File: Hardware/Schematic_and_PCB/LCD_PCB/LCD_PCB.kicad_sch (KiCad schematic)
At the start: 9 parts, among them J1 LCD_display, J2 Conn_01x03, J4 Conn_01x09, SW1 Button_down, SW2 Button_up, SW3 Button_ok, SW4 Button_back

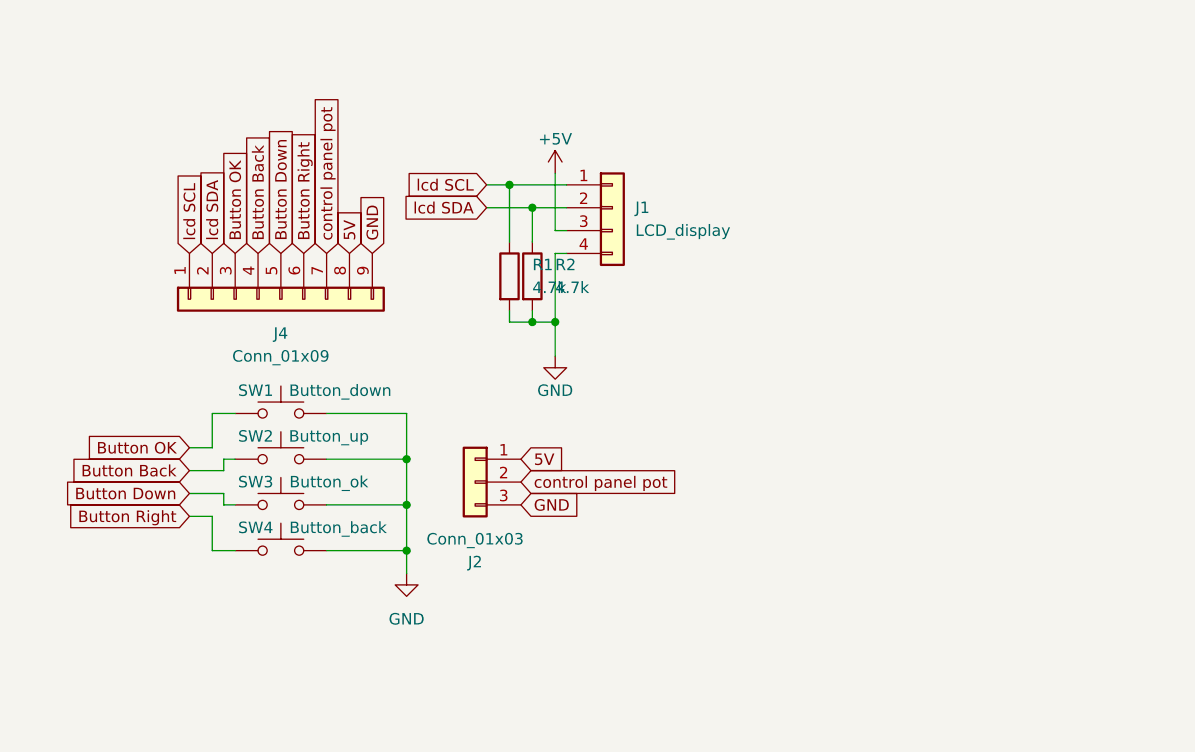
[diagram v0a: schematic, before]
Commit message: Update PCB LCD
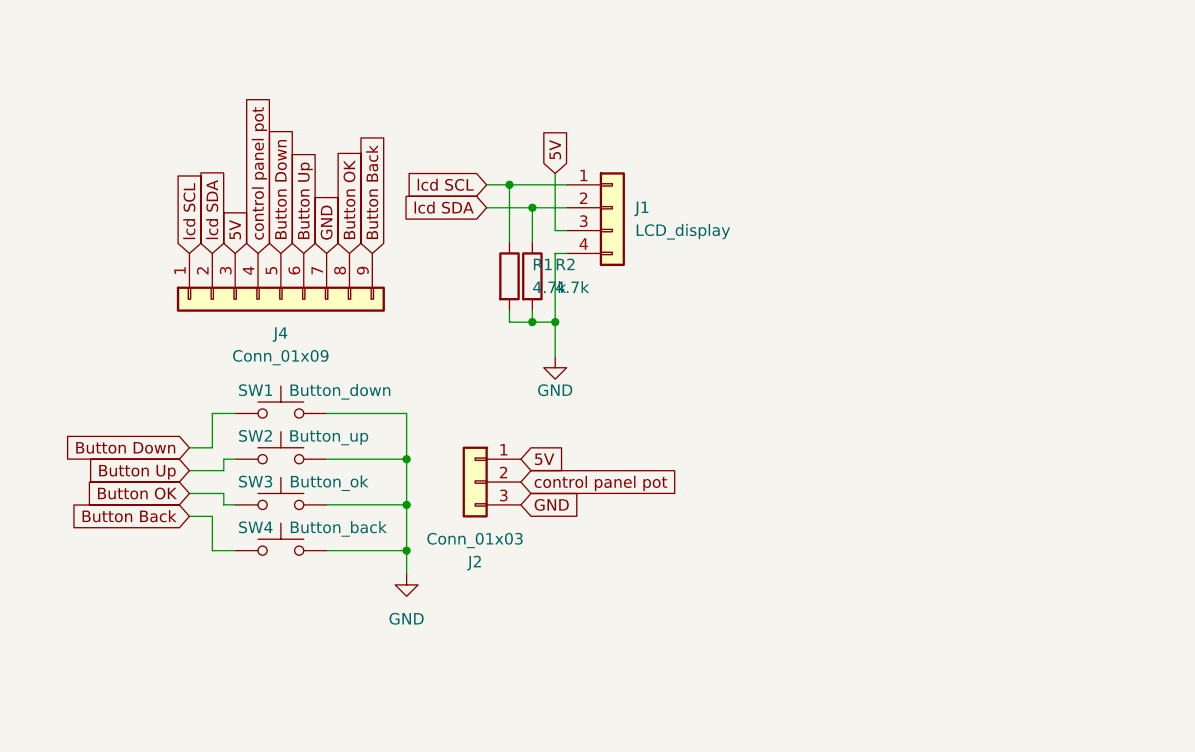
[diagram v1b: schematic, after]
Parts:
- R1, R2: footprint (none) -> Resistor_THT:R_Axial_DIN0207_L6.3mm_D2.5mm_P7.62mm_Horizontal
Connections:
- net +5V is gone; now on net 5V: J1.3 (Pin_3)
- net 5V: now also J4.3 (Pin_3); no longer J4.8 (Pin_8)
- net Button Back: now also J4.9 (Pin_9), SW4.1; no longer J4.4 (Pin_4), SW2.1
- net Button Down: now also SW1.1; no longer SW3.1
- net Button OK: now also J4.8 (Pin_8), SW3.1; no longer J4.3 (Pin_3), SW1.1
- net GND: now also J4.7 (Pin_7); no longer J4.9 (Pin_9)
- net control panel pot: now also J4.4 (Pin_4); no longer J4.7 (Pin_7)
- net Button Right renamed Button Up
- net Button Up: now also SW2.1; no longer SW4.1

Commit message: Finish LCD PCB
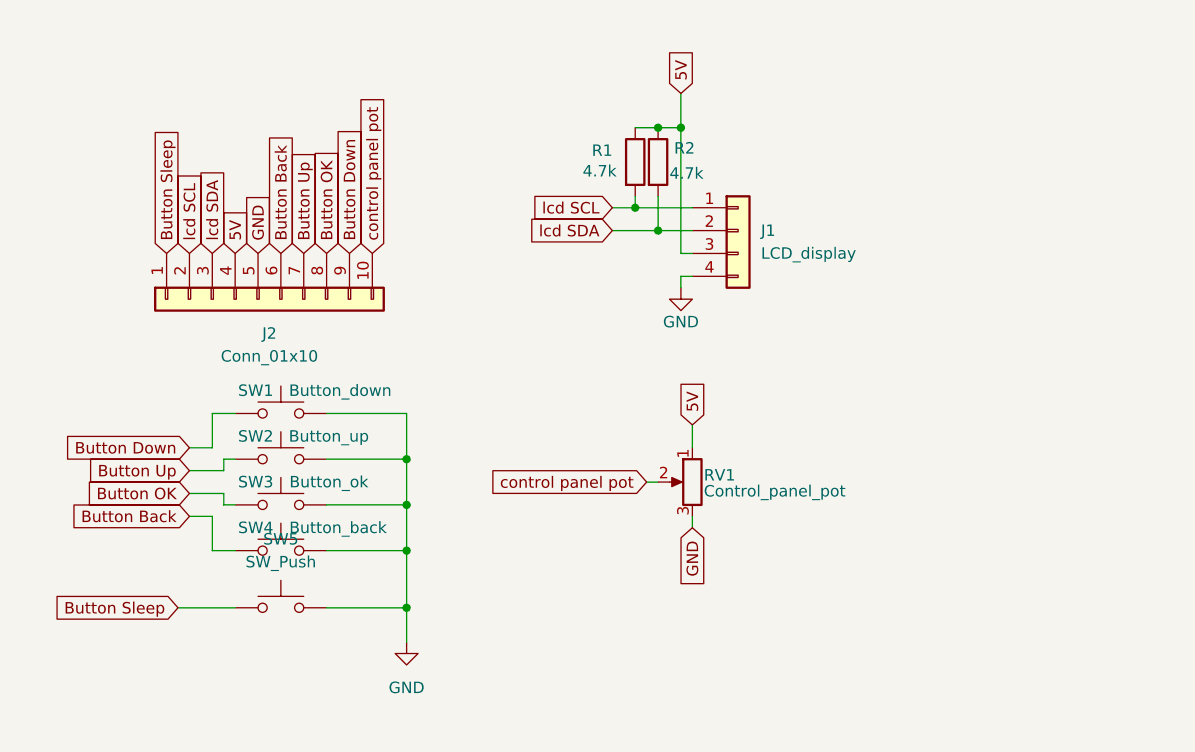
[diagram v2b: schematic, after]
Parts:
- removed J2: Conn_01x03, Connector_PinHeader_2.54mm:PinHeader_1x03_P2.54mm_Vertical, symbol Connector_Generic:Conn_01x03
- removed J4: Conn_01x09, Connector_PinHeader_2.54mm:PinHeader_1x09_P2.54mm_Vertical, symbol Connector_Generic:Conn_01x09
- added J2: Conn_01x10, Connector_PinHeader_2.54mm:PinHeader_1x10_P2.54mm_Vertical, symbol Connector_Generic:Conn_01x10
- added RV1: Control_panel_pot, Potentiometer:PDB182-K-Potentiometer, symbol Device:R_Potentiometer
- added SW5: SW_Push, Button_Switch_THT:SW_PUSH_6mm_H5mm, symbol Switch:SW_Push
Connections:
- net 5V: now also R1.1, R2.1, J2.4 (Pin_4), RV1.1
- net Button Back: now also J2.6 (Pin_6)
- net Button Down: now also J2.9 (Pin_9)
- net Button OK: now also J2.8 (Pin_8)
- net Button Up: now also J2.7 (Pin_7)
- net GND: now also J2.5 (Pin_5), RV1.3, SW5.2; no longer R1.2, R2.2
- net control panel pot: now also J2.10 (Pin_10), RV1.2
- net lcd SCL: now also R1.2, J2.2 (Pin_2); no longer R1.1
- net lcd SDA: now also R2.2, J2.3 (Pin_3); no longer R2.1
- new net Button Sleep: J2.1 (Pin_1), SW5.1
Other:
- moved on the sheet: J1, R1, R2

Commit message: Update bunch of stuff
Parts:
- RV1: footprint Potentiometer:PDB182-K-Potentiometer -> Potentiometer:PDB182-K-Potentiometer-Horizontal
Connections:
- net 5V: now also J2.2 (Pin_2), RV1.3; no longer J2.4 (Pin_4), RV1.1
- net Button Back: now also J2.4 (Pin_4); no longer J2.6 (Pin_6)
- net Button Down: now also J2.5 (Pin_5); no longer J2.9 (Pin_9)
- net Button OK: now also J2.6 (Pin_6); no longer J2.8 (Pin_8)
- net Button Sleep: now also J2.3 (Pin_3); no longer J2.1 (Pin_1)
- net GND: now also J2.8 (Pin_8), RV1.1; no longer J2.5 (Pin_5), RV1.3
- net control panel pot: now also J2.1 (Pin_1); no longer J2.10 (Pin_10)
- net lcd SCL: now also J2.9 (Pin_9); no longer J2.2 (Pin_2)
- net lcd SDA: now also J2.10 (Pin_10); no longer J2.3 (Pin_3)
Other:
- moved on the sheet: RV1

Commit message: Finalize LCD PCB
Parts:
- added H1, H2, H3, H4: MountingHole, MountingHole:MountingHole_3.2mm_M3, symbol Mechanical:MountingHole

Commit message: Code update for room 3
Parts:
- added TP1, TP2, TP3, TP4, TP5, TP6: TestPoint, TestPoint:TestPoint_Pad_1.5x1.5mm, symbol Connector:TestPoint
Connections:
- net 5V: now also TP6.1
- net Button Sleep: now also TP1.1
- net GND: now also TP5.1
- net control panel pot: now also TP2.1
- net lcd SCL: now also TP3.1
- net lcd SDA: now also TP4.1

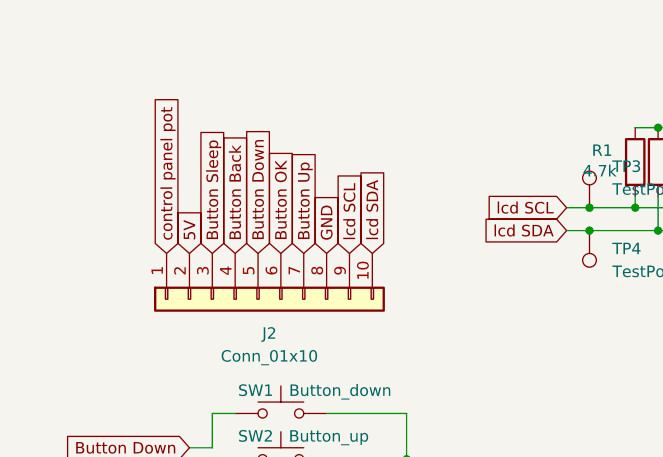
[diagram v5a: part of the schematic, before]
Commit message: Update pinout order of LCD PCB
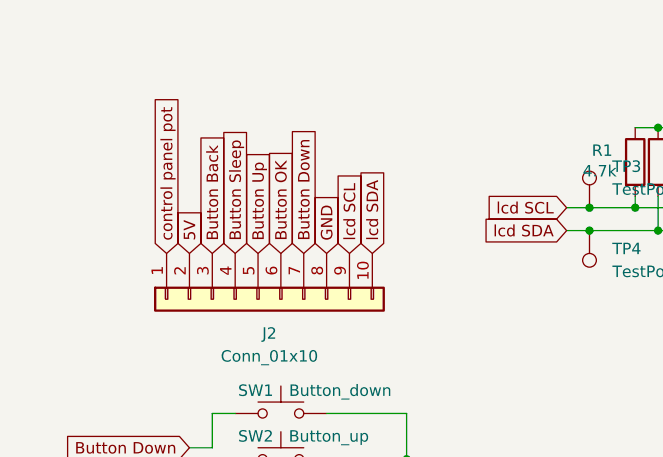
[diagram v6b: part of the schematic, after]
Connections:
- net Button Back: now also J2.3 (Pin_3); no longer J2.4 (Pin_4)
- net Button Down: now also J2.7 (Pin_7); no longer J2.5 (Pin_5)
- net Button Sleep: now also J2.4 (Pin_4); no longer J2.3 (Pin_3)
- net Button Up: now also J2.5 (Pin_5); no longer J2.7 (Pin_7)
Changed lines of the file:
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@@
 	(global_label "Button Back"
 		(shape input)
+		(at 58.42 78.74 90)
+		(fields_autoplaced yes)
+		(effects
+			(font
+				(size 1.27 1.27)
+			)
+			(justify left)
+		)
+		(property "Intersheetrefs" "${INTERSHEET_REFS}"
+			(at 58.42 64.0831 90)
+			(effects
+				(font
+					(size 1.27 1.27)
+				)
+				(justify left)
+				(hide yes)
+			)
+		)
+	)
+	(global_label "Button Up"
+		(shape input)
+		(at 55.88 102.87 180)
+		(fields_autoplaced yes)
+		(effects
+			(font
+				(size 1.27 1.27)
+			)
+			(justify right)
+		)
+		(property "Intersheetrefs" "${INTERSHEET_REFS}"
+			(at 40.8603 102.87 0)
+			(effects
+				(font
+					(size 1.27 1.27)
+				)
+				(justify right)
+				(hide yes)
+			)
+		)
+	)
+	(global_label "control panel pot"
+		(shape input)
+		(at 125.73 104.14 0)
+		(fields_autoplaced yes)
+		(effects
+			(font
+				(size 1.27 1.27)
+			)
+			(justify left)
+		)
+		(property "Intersheetrefs" "${INTERSHEET_REFS}"
+			(at 145.5876 104.14 0)
+			(effects
+				(font
+					(size 1.27 1.27)
+				)
+				(justify left)
+				(hide yes)
+			)
+		)
+	)
+	(global_label "5V"
+		(shape input)
+		(at 111.76 97.79 90)
+		(fields_autoplaced yes)
+		(effects
+			(font
+				(size 1.27 1.27)
+			)
+			(justify left)
+		)
+		(property "Intersheetrefs" "${INTERSHEET_REFS}"
+			(at 111.76 92.5067 90)
+			(effects
+				(font
+					(size 1.27 1.27)
+				)
+				(justify left)
+				(hide yes)
+			)
+		)
+	)
+	(global_label "Button Up"
+		(shape input)
+		(at 63.5 78.74 90)
+		(fields_autoplaced yes)
+		(effects
+			(font
+				(size 1.27 1.27)
+			)
+			(justify left)
+		)
+		(property "Intersheetrefs" "${INTERSHEET_REFS}"
+			(at 63.5 66.1393 90)
+			(effects
+				(font
+					(size 1.27 1.27)
+				)
+				(justify left)
+				(hide yes)
+			)
+		)
+	)
+	(global_label "lcd SCL"
+		(shape input)
+		(at 73.66 78.74 90)
+		(fields_autoplaced yes)
+		(effects
+			(font
+				(size 1.27 1.27)
+			)
+			(justify left)
+		)
+		(property "Intersheetrefs" "${INTERSHEET_REFS}"
+			(at 73.66 68.3768 90)
+			(effects
+				(font
+					(size 1.27 1.27)
+				)
+				(justify left)
+				(hide yes)
+			)
+		)
+	)
+	(global_label "lcd SDA"
+		(shape input)
+		(at 76.2 78.74 90)
+		(fields_autoplaced yes)
+		(effects
+			(font
+				(size 1.27 1.27)
+			)
+			(justify left)
+		)
+		(property "Intersheetrefs" "${INTERSHEET_REFS}"
+			(at 76.2 68.3163 90)
+			(effects
+				(font
+					(size 1.27 1.27)
+				)
+				(justify left)
+				(hide yes)
+			)
+		)
+	)
+	(global_label "Button Down"
+		(shape input)
+		(at 68.58 78.74 90)
+		(fields_autoplaced yes)
+		(effects
+			(font
+				(size 1.27 1.27)
+			)
+			(justify left)
+		)
+		(property "Intersheetrefs" "${INTERSHEET_REFS}"
+			(at 68.58 63.7203 90)
+			(effects
+				(font
+					(size 1.27 1.27)
+				)
+				(justify left)
+				(hide yes)
+			)
+		)
+	)
+	(global_label "Button Down"
+		(shape input)
+		(at 55.88 100.33 180)
+		(fields_autoplaced yes)
+		(effects
+			(font
+				(size 1.27 1.27)
+			)
+			(justify right)
+		)
+		(property "Intersheetrefs" "${INTERSHEET_REFS}"
+			(at 40.8603 100.33 0)
+			(effects
+				(font
+					(size 1.27 1.27)
+				)
+				(justify right)
+				(hide yes)
+			)
+		)
+	)
+	(global_label "Button Sleep"
+		(shape input)
 		(at 60.96 78.74 90)
 		(fields_autoplaced yes)
@@
 		)
 		(property "Intersheetrefs" "${INTERSHEET_REFS}"
-			(at 60.96 64.0831 90)
-			(effects
-				(font
-					(size 1.27 1.27)
-				)
-				(justify left)
-				(hide yes)
-			)
-		)
-	)
-	(global_label "Button Up"
-		(shape input)
-		(at 55.88 102.87 180)
-		(fields_autoplaced yes)
-		(effects
-			(font
-				(size 1.27 1.27)
-			)
-			(justify right)
-		)
-		(property "Intersheetrefs" "${INTERSHEET_REFS}"
-			(at 40.8603 102.87 0)
-			(effects
-				(font
-					(size 1.27 1.27)
-				)
-				(justify right)
-				(hide yes)
-			)
-		)
-	)
-	(global_label "control panel pot"
-		(shape input)
-		(at 125.73 104.14 0)
-		(fields_autoplaced yes)
-		(effects
-			(font
-				(size 1.27 1.27)
-			)
-			(justify left)
-		)
-		(property "Intersheetrefs" "${INTERSHEET_REFS}"
-			(at 145.5876 104.14 0)
-			(effects
-				(font
-					(size 1.27 1.27)
-				)
-				(justify left)
-				(hide yes)
-			)
-		)
-	)
-	(global_label "5V"
-		(shape input)
-		(at 111.76 97.79 90)
-		(fields_autoplaced yes)
-		(effects
-			(font
-				(size 1.27 1.27)
-			)
-			(justify left)
-		)
-		(property "Intersheetrefs" "${INTERSHEET_REFS}"
-			(at 111.76 92.5067 90)
-			(effects
-				(font
-					(size 1.27 1.27)
-				)
-				(justify left)
-				(hide yes)
-			)
-		)
-	)
-	(global_label "Button Up"
-		(shape input)
-		(at 68.58 78.74 90)
-		(fields_autoplaced yes)
-		(effects
-			(font
-				(size 1.27 1.27)
-			)
-			(justify left)
-		)
-		(property "Intersheetrefs" "${INTERSHEET_REFS}"
-			(at 68.58 66.1393 90)
-			(effects
-				(font
-					(size 1.27 1.27)
-				)
-				(justify left)
-				(hide yes)
-			)
-		)
-	)
-	(global_label "lcd SCL"
-		(shape input)
-		(at 73.66 78.74 90)
-		(fields_autoplaced yes)
-		(effects
-			(font
-				(size 1.27 1.27)
-			)
-			(justify left)
-		)
-		(property "Intersheetrefs" "${INTERSHEET_REFS}"
-			(at 73.66 68.3768 90)
-			(effects
-				(font
-					(size 1.27 1.27)
-				)
-				(justify left)
-				(hide yes)
-			)
-		)
-	)
-	(global_label "lcd SDA"
-		(shape input)
-		(at 76.2 78.74 90)
-		(fields_autoplaced yes)
-		(effects
-			(font
-				(size 1.27 1.27)
-			)
-			(justify left)
-		)
-		(property "Intersheetrefs" "${INTERSHEET_REFS}"
-			(at 76.2 68.3163 90)
-			(effects
-				(font
-					(size 1.27 1.27)
-				)
-				(justify left)
-				(hide yes)
-			)
-		)
-	)
-	(global_label "Button Down"
-		(shape input)
-		(at 63.5 78.74 90)
-		(fields_autoplaced yes)
-		(effects
-			(font
-				(size 1.27 1.27)
-			)
-			(justify left)
-		)
-		(property "Intersheetrefs" "${INTERSHEET_REFS}"
-			(at 63.5 63.7203 90)
-			(effects
-				(font
-					(size 1.27 1.27)
-				)
-				(justify left)
-				(hide yes)
-			)
-		)
-	)
-	(global_label "Button Down"
-		(shape input)
-		(at 55.88 100.33 180)
-		(fields_autoplaced yes)
-		(effects
-			(font
-				(size 1.27 1.27)
-			)
-			(justify right)
-		)
-		(property "Intersheetrefs" "${INTERSHEET_REFS}"
-			(at 40.8603 100.33 0)
-			(effects
-				(font
-					(size 1.27 1.27)
-				)
-				(justify right)
-				(hide yes)
-			)
-		)
-	)
-	(global_label "Button Sleep"
-		(shape input)
-		(at 58.42 78.74 90)
-		(fields_autoplaced yes)
-		(effects
-			(font
-				(size 1.27 1.27)
-			)
-			(justify left)
-		)
-		(property "Intersheetrefs" "${INTERSHEET_REFS}"
-			(at 58.42 63.4179 90)
-			(effects
-				(font
+			(at 60.96 63.4179 90)
+			(effects
+				(font

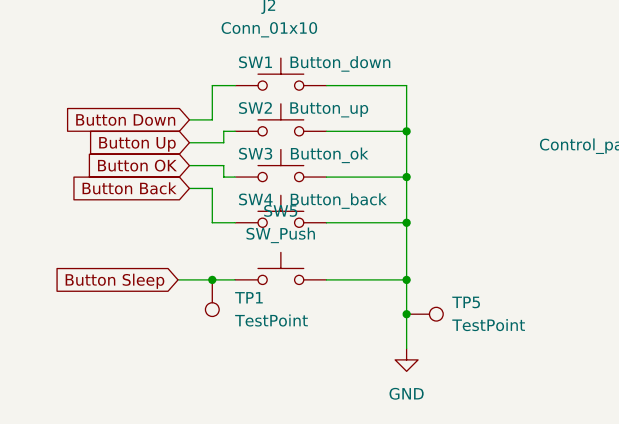
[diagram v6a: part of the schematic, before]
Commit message: Made the LCD PCB Schematic better readable
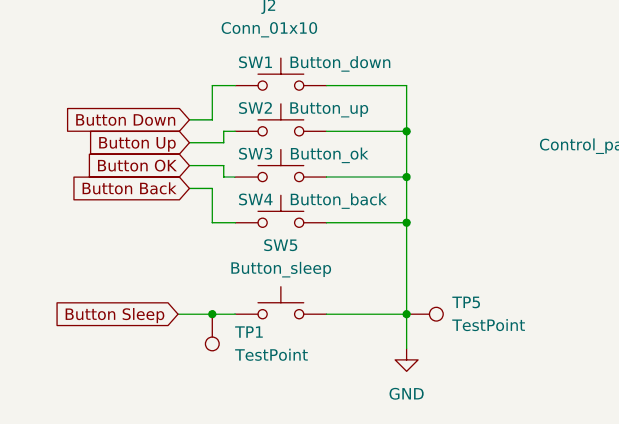
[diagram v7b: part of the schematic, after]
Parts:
- SW5: value SW_Push -> Button_sleep
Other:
- moved on the sheet: SW5, TP1
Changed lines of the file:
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@@
 	(paper "A4")
+	(junction
+		(at 58.42 121.92)
+		(diameter 0)
+		(color 0 0 0 0)
+	)
 	(junction
 		(at 100.33 73.66)
@@
 	)
 	(junction
-		(at 58.42 118.11)
-		(diameter 0)
-		(color 0 0 0 0)
-	)
-	(junction
-		(at 80.01 118.11)
-		(diameter 0)
-		(color 0 0 0 0)
-	)
-	(junction
 		(at 107.95 76.2)
 		(diameter 0)
@@
 	(wire
 		(pts
-			(xy 80.01 121.92) (xy 80.01 118.11)
+			(xy 58.42 121.92) (xy 60.96 121.92)
 		)
 		(stroke
@@
 	(wire
 		(pts
-			(xy 80.01 118.11) (xy 80.01 111.76)
-		)
-		(stroke
-			(width 0)
-			(type default)
-		)
-	)
-	(wire
-		(pts
 			(xy 125.73 104.14) (xy 119.38 104.14)
 		)
@@
 	(wire
 		(pts
-			(xy 54.61 118.11) (xy 58.42 118.11)
+			(xy 54.61 121.92) (xy 58.42 121.92)
+		)
+		(stroke
+			(width 0)
+			(type default)
+		)
+	)
+	(wire
+		(pts
+			(xy 80.01 111.76) (xy 80.01 121.92)
 		)
 		(stroke
@@
 	(wire
 		(pts
-			(xy 71.12 118.11) (xy 80.01 118.11)
+			(xy 71.12 121.92) (xy 80.01 121.92)
 		)
 		(stroke
@@
 		(pts
 			(xy 111.76 97.79) (xy 111.76 100.33)
-		)
-		(stroke
-			(width 0)
-			(type default)
-		)
-	)
-	(wire
-		(pts
-			(xy 58.42 118.11) (xy 60.96 118.11)
 		)
 		(stroke
@@
 	(global_label "Button Sleep"
 		(shape input)
-		(at 54.61 118.11 180)
+		(at 54.61 121.92 180)
 		(fields_autoplaced yes)
 		(effects
@@
 		)
 		(property "Intersheetrefs" "${INTERSHEET_REFS}"
-			(at 39.2879 118.11 0)
+			(at 39.2879 121.92 0)
 			(effects
 				(font
@@
 	(symbol
 		(lib_id "Switch:SW_Push")
-		(at 66.04 118.11 0)
+		(at 66.04 121.92 0)
 		(unit 1)
 		(exclude_from_sim no)
@@
 		(fields_autoplaced yes)
 		(property "Reference" "SW5"
-			(at 66.04 110.49 0)
-			(effects
-				(font
-					(size 1.27 1.27)
-				)
-			)
-		)
-		(property "Value" "SW_Push"
-			(at 66.04 113.03 0)
+			(at 66.04 114.3 0)
+			(effects
+				(font
+					(size 1.27 1.27)
+				)
+			)
+		)
+		(property "Value" "Button_sleep"
+			(at 66.04 116.84 0)
 			(effects
 				(font
@@
 		)
 		(property "Footprint" "Button_Switch_THT:SW_PUSH_6mm_H5mm"
-			(at 66.04 113.03 0)
+			(at 66.04 116.84 0)
 			(effects
 				(font
@@
 		)
 		(property "Datasheet" "~"
-			(at 66.04 113.03 0)
+			(at 66.04 116.84 0)
 			(effects
 				(font
@@
 		)
 		(property "Description" "Push button switch, generic, two pins"
-			(at 66.04 118.11 0)
+			(at 66.04 121.92 0)
 			(effects
 				(font
@@
 	(symbol
 		(lib_id "Connector:TestPoint")
-		(at 58.42 118.11 180)
+		(at 58.42 121.92 180)
 		(unit 1)
 		(exclude_from_sim no)
@@
 		(fields_autoplaced yes)
 		(property "Reference" "TP1"
-			(at 60.96 120.1419 0)
+			(at 60.96 123.9519 0)
 			(effects
 				(font
@@
 		)
 		(property "Value" "TestPoint"
-			(at 60.96 122.6819 0)
+			(at 60.96 126.4919 0)
 			(effects
 				(font
@@
 		)
 		(property "Footprint" "TestPoint:TestPoint_Pad_1.5x1.5mm"
-			(at 53.34 118.11 0)
+			(at 53.34 121.92 0)
 			(effects
 				(font
@@
 		)
 		(property "Datasheet" "~"
-			(at 53.34 118.11 0)
+			(at 53.34 121.92 0)
 			(effects
 				(font
@@
 		)
 		(property "Description" "test point"
-			(at 58.42 118.11 0)
-			(effects
-				(font
+			(at 58.42 121.92 0)
+			(effects
+				(font

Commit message: Some changes related to pdf export.
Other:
- title: (none) -> Control panel
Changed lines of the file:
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@@
 	(generator_version "8.0")
 	(paper "A4")
+	(title_block
+		(title "Control panel")
+		(date "2024-12-28")
+		(rev "1.0.0")
+	)
 	(junction
 		(at 58.42 121.92)
